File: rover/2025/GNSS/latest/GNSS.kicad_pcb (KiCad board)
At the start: 4 copper layers, 50 x 50 mm, 42 parts, among them J1 Eth-Horiz, J2 Eth-Horiz, J4 JST6_Pin, J5 USB_C_USB4145-GCT, SW1 TS09-63-25-WT-160-SMT-TR, SW2 TS09-63-25-WT-160-SMT-TR, U1 SN65HVD232, U2 ESP32-S3-WROVER, U4 LDO-TLV74033PDBVR, U5 TVS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

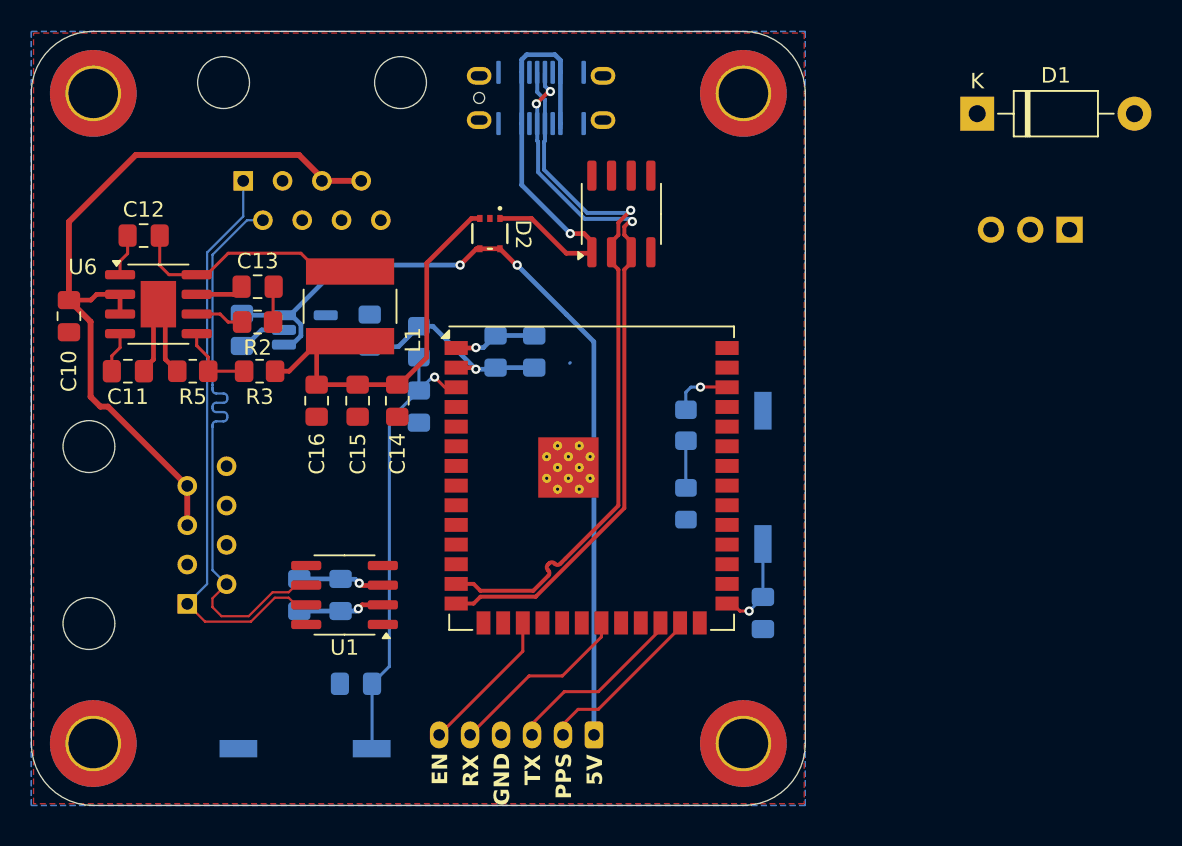
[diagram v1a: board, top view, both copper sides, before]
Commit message: gnss modif
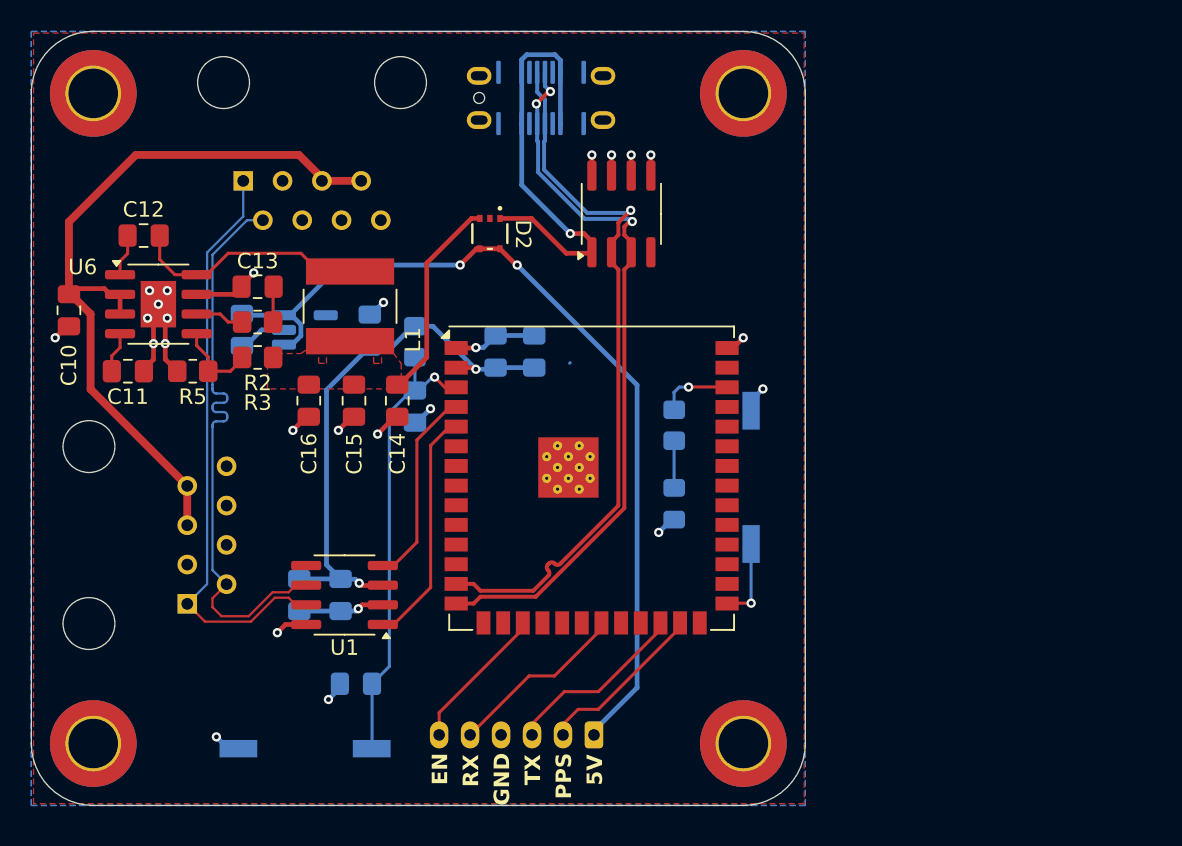
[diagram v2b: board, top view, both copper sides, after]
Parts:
- removed C2: 100nF, Capacitor_SMD:C_0805_2012Metric_Pad1.18x1.45mm_HandSolder
- removed D1: SB140, Diode_THT:D_DO-41_SOD81_P10.16mm_Horizontal
- removed JP1: Selector-Jumper_3_Open, Connector_PinHeader_2.54mm:PinHeader_1x03_P2.54mm_Vertical
- moved R3 0.90 mm to (142.6, 91.1)
- moved D3 0.76 mm to (169.5, 100.5)
- moved R4 0.76 mm to (169.5, 95.4)
- moved SW2 0.76 mm to (174.5, 98.8)
- moved C16 0.51 mm to (145.9, 93.9)
- moved C10 0.38 mm to (130.4, 88.0)
- moved C7 0.25 mm to (152.8, 94.2)
- moved R1 0.25 mm to (152.8, 90.0)
- moved C15 0.24 mm to (148.8, 93.9)
- moved G*** 0.13 mm to (134.5, 92.1)
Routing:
- net GND: track 26.8 -> 54.8 mm, vias 2 -> 26
- net +3.3V: track 21.9 -> 38.5 mm
- net RXC: track 0.00 -> 15.4 mm
- net TXC: track 0.00 -> 12.8 mm
- net +5V_ETH: track 31.2 -> 19.6 mm
- net +5V: track 55.8 -> 58.2 mm
- net GPIO_0: track 6.33 -> 5.39 mm
- net LED_BUILDIN: track 3.89 -> 4.67 mm
- added copper zone on F.Cu, net +5V_ETH
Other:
- board text added: "GNSS REV1 by: J.Y.P. & L.P. 2025-06-17 Robotique UdeS ROVUS"
- board text removed: "ETH--USB"
- board text removed: "GNSS REV1 by: JUNE YOUNG PARK 2025-03-12 Robotique UdeS ROVUS"
- board text removed: "PWR"

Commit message: gnss update
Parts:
- added U3: Volt_check-NCV308, Package_SO:TSOP-6_1.65x3.05mm_P0.95mm, B.Cu at (148.5, 98.7)
- C13, R2: moved to B.Cu
- moved L1 4.61 mm to (144.0, 87.2)
- moved C5 2.48 mm to (149.7, 91.8)
- moved U4 2.48 mm to (145.5, 91.8)
- moved C6 2.48 mm to (141.4, 91.8)
- moved R3 1.26 mm to (142.6, 92.3)
- moved C14 0.62 mm to (151.7, 93.2)
- moved C15 0.62 mm to (148.9, 93.2)
- moved C16 0.62 mm to (146.0, 93.2)
- moved C11 0.37 mm to (134.2, 92.3)
- moved R5 0.37 mm to (138.4, 92.3)
- moved C10 0.24 mm to (130.4, 88.3)
- moved C12 0.24 mm to (135.2, 83.4)
- moved U6 0.24 mm to (136.2, 87.9)
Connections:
- C1 pad 1: EN_ESP -> EN_SW
- SW1 pad 1: EN_ESP -> EN_SW
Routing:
- net EN_ESP: track 29.9 -> 11.4 mm
- net EN_SW: track 0.00 -> 17.8 mm
- net Net-(U6-SW): track 15.3 -> 4.99 mm
- net +5V: track 58.2 -> 64.6 mm
- net +5V_ETH: track 19.6 -> 13.2 mm
- net Net-(U6-COMB): track 3.15 -> 3.53 mm, vias 0 -> 1
- net GND: vias 26 -> 27
- added copper zone on F.Cu, net Net-(U6-SW)

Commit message: ..
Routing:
- net GND: track 54.8 -> 56.2 mm
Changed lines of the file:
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@@
 	)
 	(via
-		(at 150.53 90.219)
+		(at 150.622 88.646)
 		(size 0.6)
 		(drill 0.3)
@@
 	)
 	(segment
+		(start 150.622 89.897)
+		(end 150.622 88.646)
+		(width 0.3048)
+		(layer "B.Cu")
+		(net 1)
+	)
+	(segment
 		(start 141.24 86.5245)
 		(end 141.2025 86.487)
@@
 	)
 	(segment
-		(start 149.7565 90.7625)
-		(end 150.542 89.977)
-		(width 0.3048)
-		(layer "B.Cu")
-		(net 1)
-	)
-	(segment
 		(start 141.377 116.332)
 		(end 140.716 116.332)
@@
 		(width 0.3048)
 		(layer "B.Cu")
+		(net 1)
+	)
+	(segment
+		(start 149.7565 90.7625)
+		(end 150.622 89.897)
+		(width 0.3048)
+		(layer "B.Cu")

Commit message: update gnss
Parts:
- added R6: 5k1, Resistor_SMD:R_0805_2012Metric_Pad1.20x1.40mm_HandSolder, F.Cu at (157.9, 80.8)
- added R7: 5k1, Resistor_SMD:R_0805_2012Metric_Pad1.20x1.40mm_HandSolder, F.Cu at (168.4, 74.0)
- moved D2 0.89 mm to (157.6, 83.9)
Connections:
- J5 pad A5: unconnected-(J5-CC1-PadA5) -> Net-(J5-CC1)
- J5 pad B5: unconnected-(J5-CC2-PadB5) -> Net-(J5-CC2)
- J5 pad S1: unconnected-(J5-SHIELD-PadS1)_3 -> GND
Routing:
- net Net-(J5-CC2): track 0.00 -> 8.92 mm, vias 0 -> 1
- net Net-(J5-CC1): track 0.00 -> 6.11 mm, vias 0 -> 1
- net +5V_USB: track 28.9 -> 29.9 mm
- net +5V: track 64.6 -> 63.8 mm

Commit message: gnss rev1 commande
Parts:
- SW1, SW2: footprint Button_Switch_SMD:SW_DIP_SPSTx01_Slide_6.7x4.1mm_W8.61mm_P2.54mm_LowProfile -> RoverFootprint:SW-PTS815 SJM250SMTRLFS
- moved C1 1.42 mm to (147.6, 112.4)
- moved SW1 1.28 mm to (146.9, 116.1), turned to 0 degrees
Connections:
- SW1 pad 1: EN_SW -> GND
- SW2 pad 2: GPIO_0 -> GND
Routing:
- net GND: track 56.2 -> 52.4 mm, vias 27 -> 25
- net GPIO_0: track 5.39 -> 7.89 mm

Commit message: footprint update
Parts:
- moved D2 0.30 mm to (157.6, 84.2)
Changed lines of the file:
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@@
 	(footprint "RoverFootprint:Diode_schottky-CVJ10F30"
 		(layer "F.Cu")
-		(at 157.607 83.947 -90)
+		(at 157.607 84.25 -90)
 		(tags "CVJ10F30_LF ")
 		(property "Reference" "D2"
@@
 			)
 		)
-		(property "Status" "TO BE VERIFIED"
-			(at 0 0 270)
-			(unlocked yes)
-			(layer "F.Fab")
-			(hide yes)
-			(effects
-				(font
-					(size 1 1)
-					(thickness 0.15)
-				)
-			)
-		)
 		(sheetname "/")
 		(sheetfile "GNSS.kicad_sch")
@@
 			)
 		)
-		(pad "1" smd rect
-			(at -0.9779 -0.649999 270)
-			(size 0.4572 0.3556)
+		(pad "1" smd roundrect
+			(at -1.24965 -0.649999 270)
+			(size 1.0007 0.3556)
 			(layers "F.Cu" "F.Mask" "F.Paste")
+			(roundrect_rratio 0.25)
 			(net 14 "+5V_USB")
 			(pintype "passive")
 		)
-		(pad "2" smd rect
-			(at -0.9779 0 270)
-			(size 0.4572 0.3556)
+		(pad "2" smd roundrect
+			(at -1.24965 0 270)
+			(size 1.0007 0.3556)
 			(layers "F.Cu" "F.Mask" "F.Paste")
+			(roundrect_rratio 0.25)
 			(net 64 "unconnected-(D2-NC-Pad2)")
 			(pinfunction "NC")
 			(pintype "passive")
 		)
-		(pad "3" smd rect
-			(at -0.9779 0.649999 270)
-			(size 0.4572 0.3556)
+		(pad "3" smd roundrect
+			(at -1.24965 0.649999 270)
+			(size 1.0007 0.3556)
 			(layers "F.Cu" "F.Mask" "F.Paste")
+			(roundrect_rratio 0.25)
 			(net 56 "+5V_ETH")
 			(pintype "passive")
 		)
-		(pad "4" smd rect
-			(at 0.9779 0.649999 270)
-			(size 0.4572 0.3556)
+		(pad "4" smd roundrect
+			(at 1.24965 0.663899 270)
+			(size 1.0007 0.327798)
 			(layers "F.Cu" "F.Mask" "F.Paste")
+			(roundrect_rratio 0.25)
 			(net 3 "+5V")
 			(pintype "passive")
 		)
-		(pad "5" smd rect
-			(at 0.9779 -0.649999 270)
-			(size 0.4572 0.3556)
+		(pad "5" smd roundrect
+			(at 1.24965 -0.649999 270)
+			(size 1.0007 0.3556)
 			(layers "F.Cu" "F.Mask" "F.Paste")
+			(roundrect_rratio 0.25)
 			(net 3 "+5V")
 			(pintype "passive")
@@
 			(keep_text_aligned yes)
 		)
-		(gr_text "1968.5039 mils"
+		(gr_text "50.0000 mm"
 			(at 153 130.675999 0)
 			(layer "User.1")
@@
 			(keep_text_aligned yes)
 		)
-		(gr_text "1653.5433 mils"
+		(gr_text "42.0000 mm"
 			(at 182.111 95 90)
 			(layer "User.1")
@@
 			(keep_text_aligned yes)
 		)
-		(gr_text "1968.5039 mils"
+		(gr_text "50.0000 mm"
 			(at 185.667 95 90)
 			(layer "User.1")
@@
 	)
 	(segment
-		(start 158.242 84.963)
-		(end 157.099 84.963)
+		(start 159.258 85.979)
+		(end 158.779 85.5)
 		(width 0.3048)
 		(layer "F.Cu")
@@
 	)
 	(segment
-		(start 157.099 84.963)
+		(start 156.562 85.5)
 		(end 156.083 85.979)
 		(width 0.3048)
@@
 	)
 	(segment
-		(start 159.258 85.979)
-		(end 158.242 84.963)
+		(start 158.779 85.5)
+		(end 156.562 85.5)
 		(width 0.3048)
 		(layer "F.Cu")
